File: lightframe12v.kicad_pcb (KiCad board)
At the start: 2 copper layers, 91.4 x 45.7 mm, 46 parts, among them J1 PJ-077, J2 Conn_01x06_Female, J3 Conn_01x06_Female, J4 Conn_01x06_Female, J5 Conn_01x10_Female, Q1 MMBT2222, Q2 MMBT2222, SW1 SW_Push, SW2 SW_Push, U1 ESP32-WROOM-32U, U2 TPS563207s, U3 TLC5971

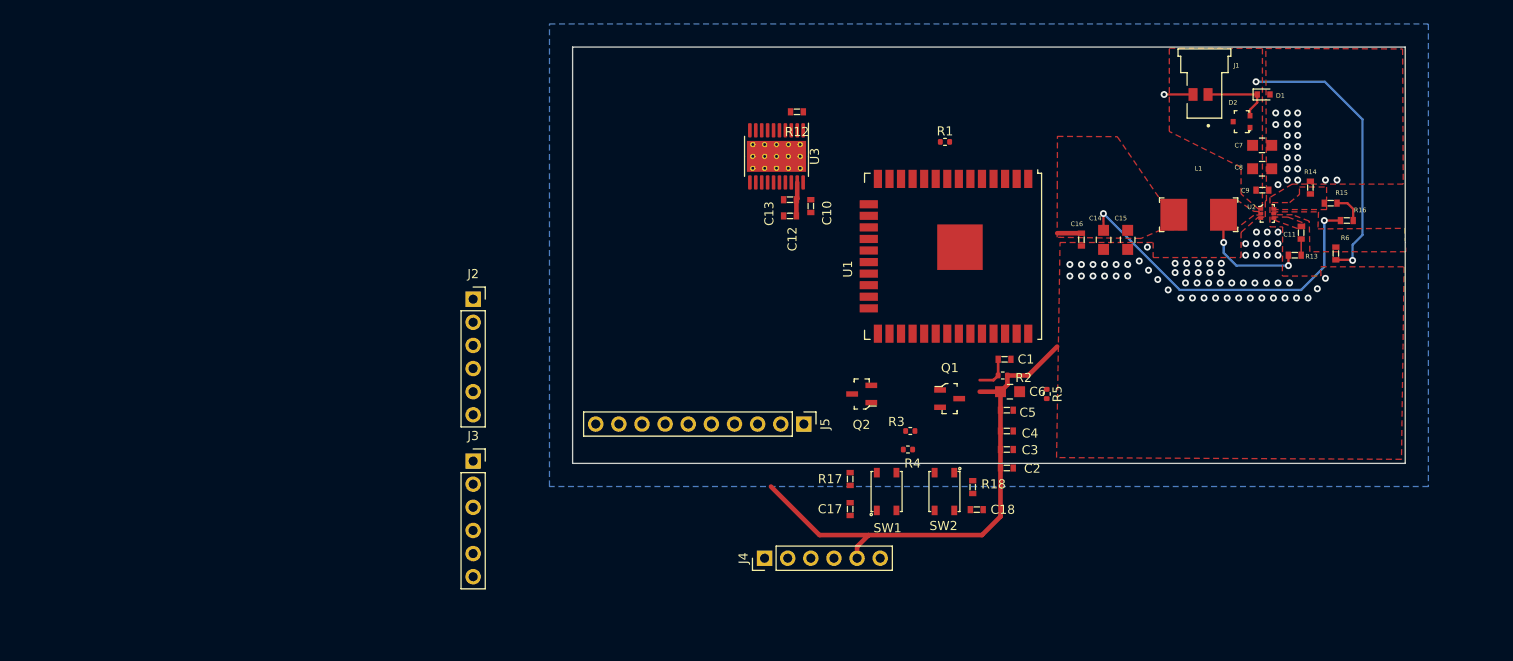
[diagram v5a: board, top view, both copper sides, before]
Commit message: Rearranges around power  traces.
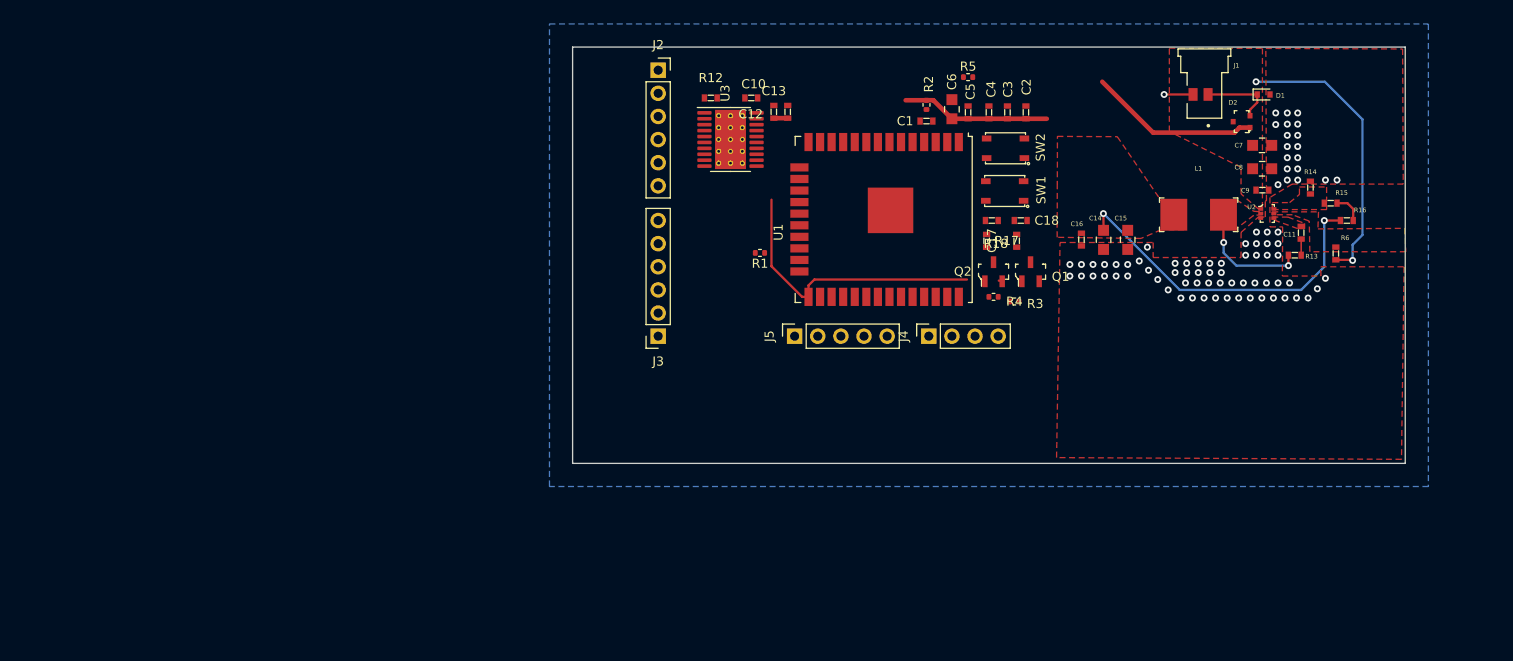
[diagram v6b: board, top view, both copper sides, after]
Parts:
- J4: value Conn_01x06_Female -> Conn_01x04_Female; footprint Connector_PinHeader_2.54mm:PinHeader_1x06_P2.54mm_Vertical -> Connector_PinSocket_2.54mm:PinSocket_1x04_P2.54mm_Vertical
- J5: value Conn_01x10_Female -> Conn_01x5_Female; footprint Connector_PinHeader_2.54mm:PinHeader_1x10_P2.54mm_Vertical -> Connector_PinSocket_2.54mm:PinSocket_1x05_P2.54mm_Vertical
- moved C2 39.1 mm to (321.6, -531.3), turned to 90 degrees
- moved SW2 38.3 mm to (319.3, -527.4), turned to 90 degrees
- moved C3 37.0 mm to (319.5, -531.3), turned to 90 degrees
- moved R5 35.9 mm to (315.2, -535.2), turned to 0 degrees
- moved SW1 35.5 mm to (319.2, -522.7), turned to 90 degrees
- moved C17 35.3 mm to (317.8, -519.4), turned to 180 degrees
- moved C4 35.0 mm to (317.5, -531.3), turned to 90 degrees
- moved C5 33.0 mm to (315.2, -531.3), turned to 90 degrees
- moved J2 32.3 mm to (281.2, -535.9)
- moved C18 32.1 mm to (321.0, -519.4)
- moved C6 31.7 mm to (313.4, -531.7), turned to 90 degrees
- moved R2 30.9 mm to (310.6, -532.1), turned to 270 degrees
- moved J4 30.3 mm to (310.9, -506.7)
- moved R17 30.2 mm to (317.2, -517.2), turned to 270 degrees
- moved C1 27.5 mm to (310.6, -530.4), turned to 180 degrees
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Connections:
- J4 pad 1: /Txd -> /Rxd
- J4 pad 2: /Rxd -> /Txd
- J5 pad 2: Net-(J5-Pad2) -> /Gpio15
- J5 pad 3: /Gpio15 -> /Gpio18
- J5 pad 4: /Gpio22 -> /Gpio19
- J5 pad 5: /Gpio23 -> /Gpio21
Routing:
- net +3V3: track 100.7 -> 56.3 mm
- net /Gpio0: track 0.00 -> 31.7 mm
- net +12V: track 31.2 -> 49.9 mm
- net /Reset: track 4.02 -> 0.00 mm

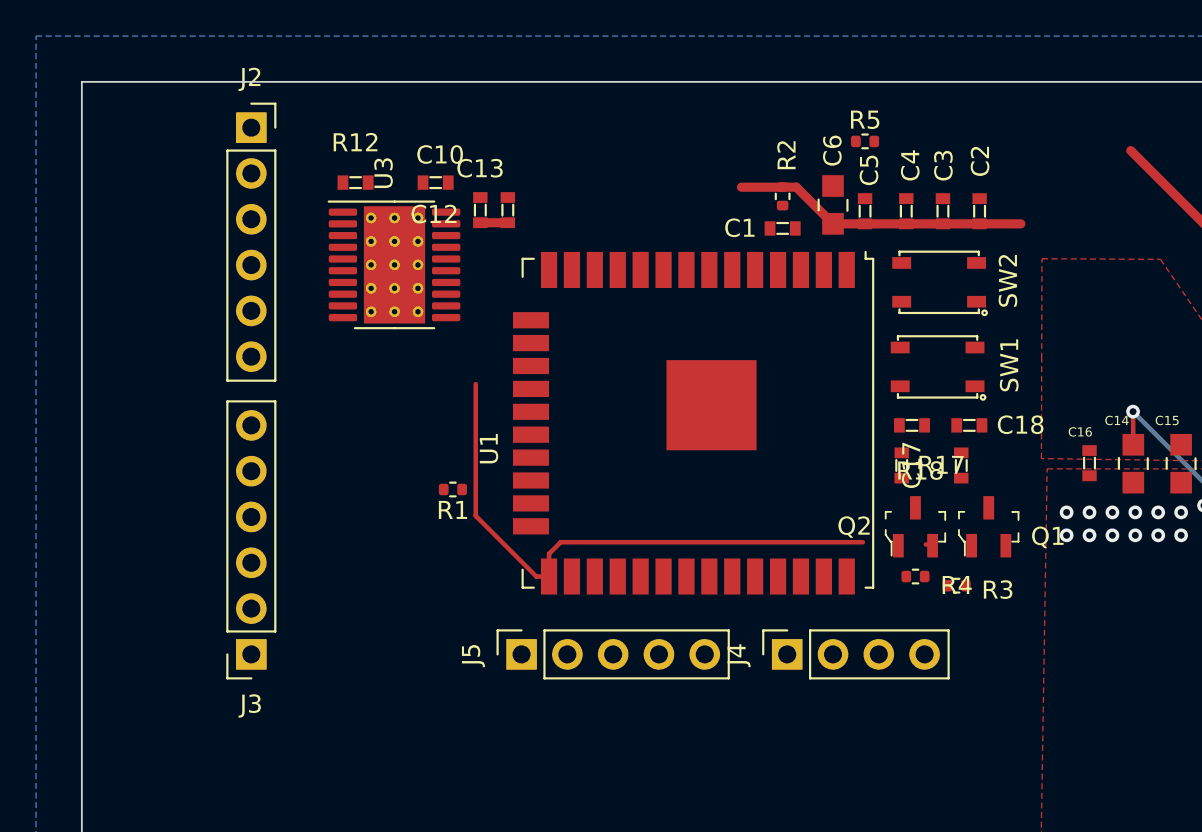
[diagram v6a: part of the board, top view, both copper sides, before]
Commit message: Moves led driver
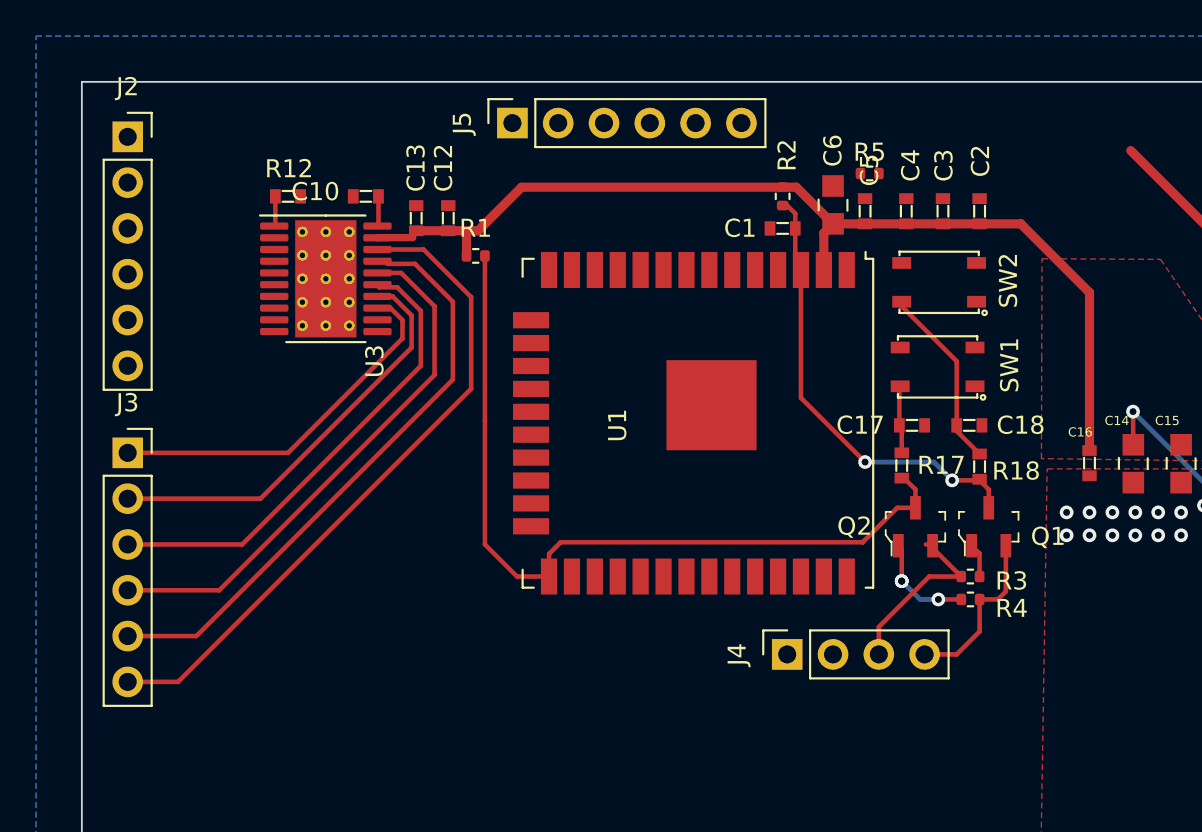
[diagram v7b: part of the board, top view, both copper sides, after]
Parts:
- J5: value Conn_01x5_Female -> Conn_01x6_Female; footprint Connector_PinSocket_2.54mm:PinSocket_1x05_P2.54mm_Vertical -> Connector_PinSocket_2.54mm:PinSocket_1x06_P2.54mm_Vertical
- moved J5 29.5 mm to (295.7, -536.2)
- moved J3 13.1 mm to (274.3, -517.9), turned to 0 degrees
- moved R1 13.0 mm to (293.6, -528.8), turned to 0 degrees
- moved J2 6.88 mm to (274.3, -535.4)
- moved C13 5.10 mm to (290.3, -530.9)
- moved C10 3.95 mm to (287.5, -532.1)
- moved U3 3.89 mm to (285.3, -527.6)
- moved R12 3.82 mm to (283.2, -532.1)
- moved R4 3.30 mm to (321.1, -509.8)
- moved C12 1.83 mm to (292.1, -530.9)
- moved R5 1.80 mm to (315.5, -533.4)
- moved R18 1.02 mm to (321.6, -517.1)
- moved R3 0.92 mm to (321.1, -511.0)
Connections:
- net /Gpio22 renamed Net-(U1-Pad36)
- net /Gpio23 renamed Net-(U1-Pad37)
- J5 pad 1: /Gpio13 -> /Gpio27
- J5 pad 2: /Gpio15 -> /Gpio26
- J5 pad 3: /Gpio18 -> /Gpio33
- J5 pad 4: /Gpio19 -> /Gpio32
- J5 pad 5: /Gpio21 -> /Gpio35
- U1 pad 11: Net-(U1-Pad11) -> /Gpio26
- U1 pad 12: Net-(U1-Pad12) -> /Gpio27
- U1 pad 16: /Serial_In -> Net-(U1-Pad16)
- U1 pad 23: /Serial_Clock -> Net-(U1-Pad23)
- U1 pad 26: Net-(U1-Pad26) -> /Serial_Clock
- U1 pad 27: /Gpio13 -> /Serial_In
- U1 pad 28: /Gpio15 -> Net-(U1-Pad28)
- U1 pad 30: /Gpio18 -> Net-(U1-Pad30)
- U1 pad 31: /Gpio19 -> Net-(U1-Pad31)
- U1 pad 33: /Gpio21 -> Net-(U1-Pad33)
- U1 pad 6: Net-(U1-Pad6) -> /Gpio34
- U1 pad 7: Net-(U1-Pad7) -> /Gpio35
- U1 pad 8: Net-(U1-Pad8) -> /Gpio32
- U1 pad 9: Net-(U1-Pad9) -> /Gpio33
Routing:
- net +3V3: track 56.3 -> 94.1 mm
- net /LED12: track 0.00 -> 37.2 mm
- net /LED11: track 0.00 -> 33.4 mm
- net /LED10: track 0.00 -> 29.7 mm
- net /LED9: track 0.00 -> 26.4 mm
- net /Reset: track 0.00 -> 24.9 mm, vias 0 -> 2
- net /LED8: track 0.00 -> 23.3 mm
- net /LED7: track 0.00 -> 20.5 mm
- net /Gpio0: track 31.7 -> 45.0 mm
- net Net-(C18-Pad2): track 0.00 -> 10.2 mm
- net /Dtr: track 0.44 -> 10.1 mm
- net /Rts: track 0.00 -> 9.53 mm
- net Net-(Q2-Pad1): track 0.00 -> 5.76 mm, vias 0 -> 3
- net Net-(C17-Pad2): track 0.00 -> 3.76 mm
- net Net-(Q1-Pad1): track 0.00 -> 1.89 mm
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
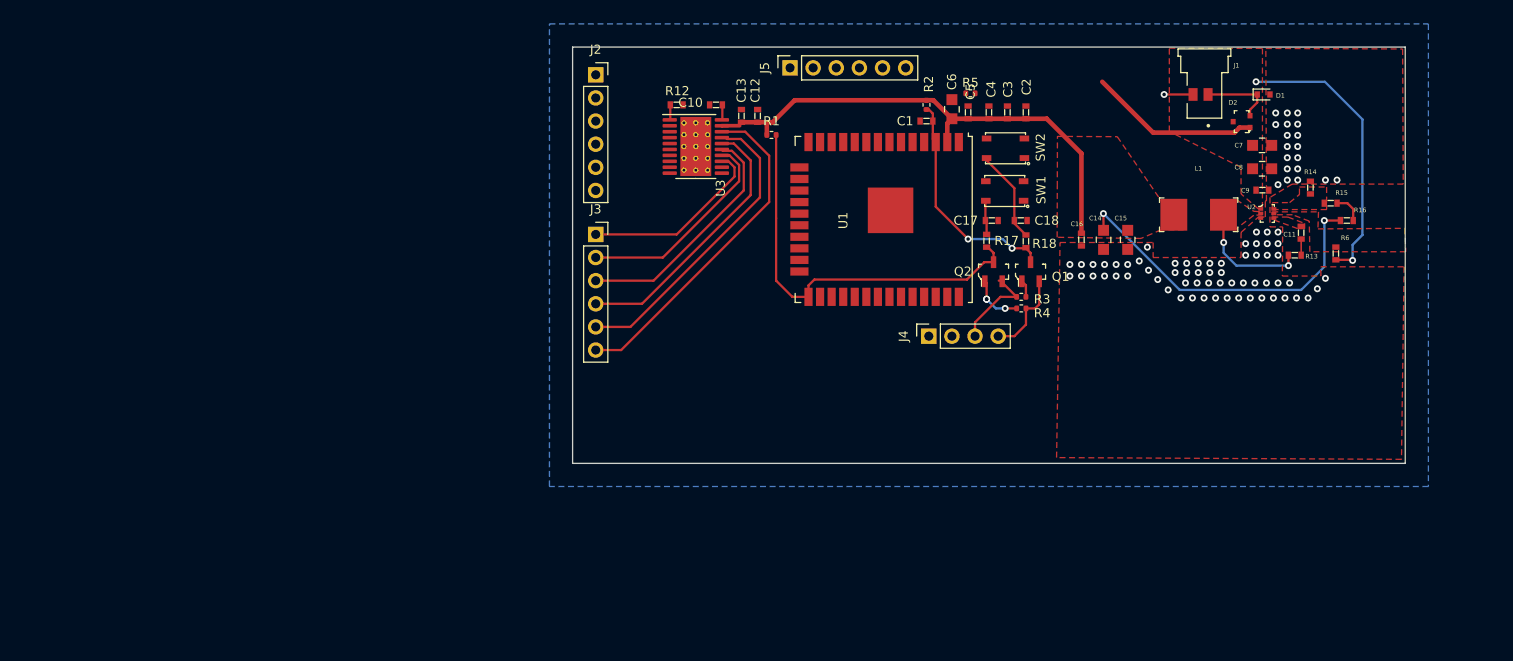
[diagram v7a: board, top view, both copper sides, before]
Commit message: rotated pmic
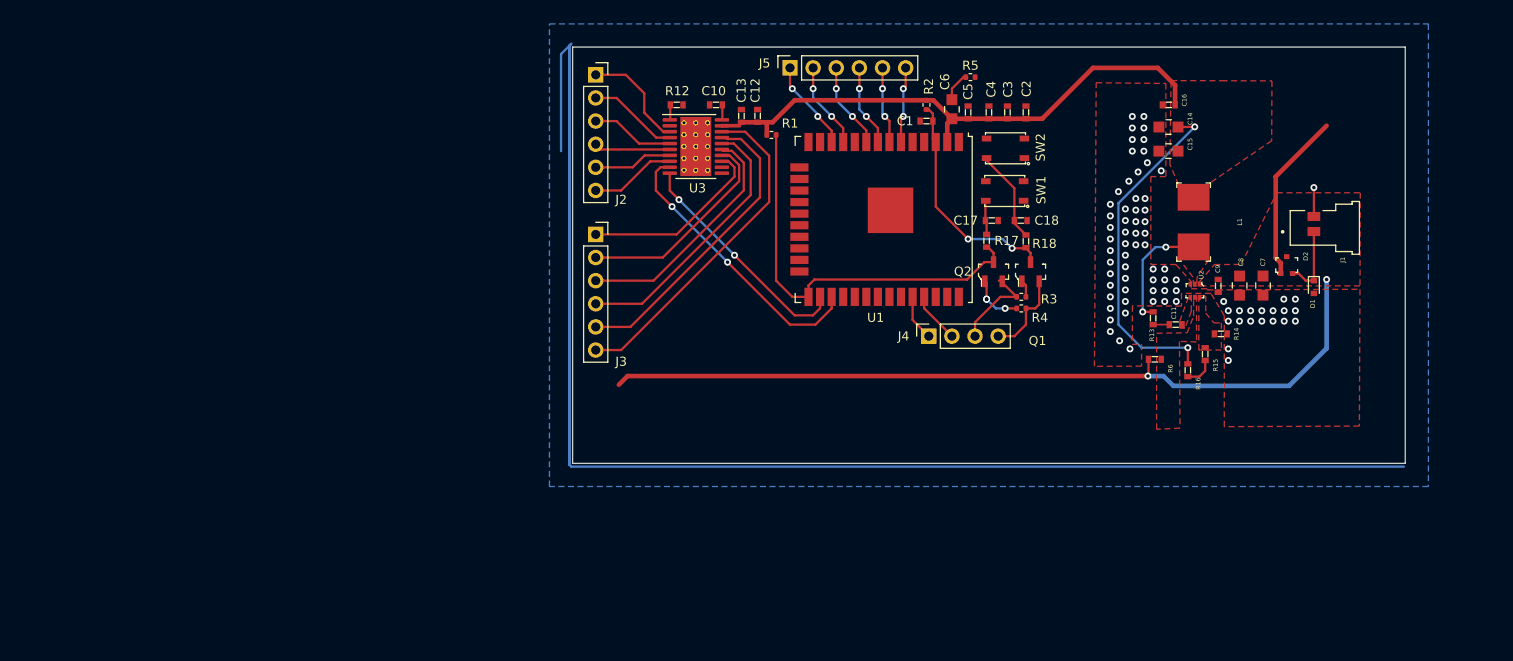
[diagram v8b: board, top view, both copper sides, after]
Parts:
- moved R16 24.0 mm to (339.3, -503.0), turned to 270 degrees
- moved R6 23.0 mm to (335.7, -504.2), turned to 0 degrees
- moved D1 21.9 mm to (353.2, -512.1), turned to 270 degrees
- moved R15 21.6 mm to (341.2, -504.8), turned to 270 degrees
- moved J1 20.8 mm to (354.5, -518.6), turned to 0 degrees
- moved R14 18.8 mm to (343.0, -507.0), turned to 0 degrees
- moved C16 17.6 mm to (337.2, -532.1), turned to 180 degrees
- moved C11 17.1 mm to (338.0, -508.0), turned to 180 degrees
- moved R13 17.0 mm to (335.5, -508.7), turned to 270 degrees
- moved D2 16.5 mm to (350.2, -514.5), turned to 90 degrees
- moved C7 15.4 mm to (347.6, -512.3), turned to 270 degrees
- moved C14 14.3 mm to (337.2, -529.7), turned to 180 degrees
- moved C8 13.1 mm to (345.0, -512.3), turned to 270 degrees
- moved U2 11.6 mm to (340.1, -511.7), turned to 180 degrees
- moved C9 11.6 mm to (342.7, -512.3), turned to 270 degrees
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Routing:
- net (no net): track 0.00 -> 196.3 mm
- net +12V: track 49.9 -> 108.4 mm
- net /Serial_In: track 0.51 -> 32.0 mm, vias 0 -> 2
- net /Serial_Clock: track 0.00 -> 25.7 mm, vias 0 -> 2
- net /LED1: track 0.00 -> 12.0 mm
- net /LED6: track 0.00 -> 10.2 mm
- net /Gpio27: track 0.00 -> 10.1 mm, vias 0 -> 2
- net /LED2: track 0.00 -> 9.93 mm
- net /Gpio33: track 0.00 -> 9.51 mm, vias 0 -> 2
- net /Gpio26: track 0.00 -> 9.51 mm, vias 0 -> 2
- net /LED3: track 0.00 -> 9.15 mm
- net /Gpio32: track 0.00 -> 8.99 mm, vias 0 -> 2
- net /LED5: track 0.00 -> 8.67 mm
- net /Gpio35: track 0.00 -> 8.46 mm, vias 0 -> 2
- net /LED4: track 0.00 -> 8.37 mm
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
